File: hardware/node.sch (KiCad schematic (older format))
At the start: 3 parts, among them U1 NRF24L01_Breakout, U2 BluePill_STM32F103C, U3 TM1637_MODULE

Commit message: Add vero desgin to hardware
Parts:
- removed U3: TM1637_MODULE, symbol TinkerForge:TM1637_MODULE
- added U3: TM1637_MODULE, SIP4, symbol bluepill_ups-rescue:TM1637_MODULE
- U1: footprint RF_Module:nRF24L01_Breakout -> SIP8; symbol Bluepill:NRF24L01_Breakout -> bluepill_ups-rescue:NRF24L01_Breakout-Bluepill
- U2: footprint BluePill_breakouts:BluePill_STM32F103C -> BLUEPILL; symbol Bluepill:BluePill_STM32F103C -> bluepill_ups-rescue:BluePill_STM32F103C-Bluepill
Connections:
- net +3V3: now also U2.18 (VCC3V3); no longer U2.40 (VCC3V3)
- net +5V: now also U3.3 (Vcc)
- net GNDREF: now also U3.4 (GND)
- net I2C1_SCL: now also U2.34 (PB6_SCL1); no longer U2.37 (PB9)
- net I2C1_SDA: now also U2.35 (PB7_SDA1); no longer U2.36 (PB8)
- new net: U2.36 (PB8), U3.1 (DIO)
- new net: U2.37 (PB9), U3.2 (CLK)
- no-connect marks 25 -> 23
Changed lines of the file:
@@
 EESchema Schematic File Version 4
+LIBS:bluepill_ups-cache
 EELAYER 26 0
 EELAYER END
@@
 $EndDescr
 $Comp
-L Bluepill:BluePill_STM32F103C U?
-U 1 1 5C14BC04
-P 5650 3750
-AR Path="/5C14BC04" Ref="U?"  Part="1"
-AR Path="/5C14BAF9/5C14BC04" Ref="U2"  Part="1"
-F 0 "U2" H 5675 2278 50  0000 C CNN
-F 1 "BluePill_STM32F103C" H 5675 2187 50  0000 C CNN
-F 2 "BluePill_breakouts:BluePill_STM32F103C" H 5700 2150 50  0001 C CNN
-F 3 "www.rogerclark.net" H 5650 2250 50  0001 C CNN
-	1    5650 3750
-	1    0    0    -1
-$EndComp
-Text Label 7650 3350 0    50   ~ 0
-I2C1_SCL
-Text Label 7650 3450 0    50   ~ 0
-I2C1_SDA
-$Comp
-L TinkerForge:TM1637_MODULE U?
-U 1 1 5C14BC0D
-P 8950 3650
-AR Path="/5C14BC0D" Ref="U?"  Part="1"
-AR Path="/5C14BAF9/5C14BC0D" Ref="U3"  Part="1"
-F 0 "U3" H 8550 4100 60  0000 L CNN
-F 1 "TM1637_MODULE" H 8900 3800 60  0000 L CNN
-F 2 "" H 8950 3650 60  0001 C CNN
-F 3 "" H 8950 3650 60  0000 C CNN
-	1    8950 3650
-	1    0    0    -1
-$EndComp
-Wire Wire Line
-	6550 3350 8350 3350
-Wire Wire Line
-	6550 3450 8350 3450
-Wire Wire Line
-	8350 3550 8250 3550
-Wire Wire Line
-	8250 3550 8250 2900
-$Comp
-L power:GNDREF #PWR?
-U 1 1 5C14BC18
-P 8250 4000
-AR Path="/5C14BC18" Ref="#PWR?"  Part="1"
-AR Path="/5C14BAF9/5C14BC18" Ref="#PWR0101"  Part="1"
-F 0 "#PWR0101" H 8250 3750 50  0001 C CNN
-F 1 "GNDREF" H 8255 3827 50  0001 C CNN
-F 2 "" H 8250 4000 50  0001 C CNN
-F 3 "" H 8250 4000 50  0001 C CNN
-	1    8250 4000
-	1    0    0    -1
-$EndComp
-Wire Wire Line
-	8350 3650 8250 3650
-Wire Wire Line
-	8250 3650 8250 4000
-$Comp
-L Bluepill:NRF24L01_Breakout U?
+L bluepill_ups-rescue:NRF24L01_Breakout-Bluepill U?
 U 1 1 5C14BC20
 P 2150 4150
@@
 F 0 "U1" H 2628 4128 50  0000 L CNN
 F 1 "NRF24L01_Breakout" H 2628 4037 50  0000 L CNN
-F 2 "RF_Module:nRF24L01_Breakout" H 2300 4750 50  0001 L CIN
+F 2 "SIP8" H 2300 4750 50  0001 L CIN
 F 3 "http://www.nordicsemi.com/eng/content/download/2730/34105/file/nRF24L01_Product_Specification_v2_0.pdf" H 2150 4050 50  0001 C CNN
 	1    2150 4150
@@
 	1    0    0    -1
 $EndComp
-$Comp
-L power:+5V #PWR?
-U 1 1 5C14BC3A
-P 6650 3250
-AR Path="/5C14BC3A" Ref="#PWR?"  Part="1"
-AR Path="/5C14BAF9/5C14BC3A" Ref="#PWR0104"  Part="1"
-F 0 "#PWR0104" H 6650 3100 50  0001 C CNN
-F 1 "+5V" V 6650 3400 50  0000 L CNN
-F 2 "" H 6650 3250 50  0001 C CNN
-F 3 "" H 6650 3250 50  0001 C CNN
-	1    6650 3250
-	0    1    1    0
-$EndComp
-$Comp
-L power:GNDREF #PWR?
-U 1 1 5C14BC40
-P 7000 3150
-AR Path="/5C14BC40" Ref="#PWR?"  Part="1"
-AR Path="/5C14BAF9/5C14BC40" Ref="#PWR0105"  Part="1"
-F 0 "#PWR0105" H 7000 2900 50  0001 C CNN
-F 1 "GNDREF" H 7005 2977 50  0001 C CNN
-F 2 "" H 7000 3150 50  0001 C CNN
-F 3 "" H 7000 3150 50  0001 C CNN
-	1    7000 3150
-	0    -1   -1   0
-$EndComp
-Wire Wire Line
-	7000 3150 6550 3150
-Wire Wire Line
-	6650 3250 6550 3250
 Text Label 3250 3850 0    50   ~ 0
 SP1_CS
@@
 L power:+3.3V #PWR?
 U 1 1 5C14BC55
-P 6650 3050
+P 4400 4750
 AR Path="/5C14BC55" Ref="#PWR?"  Part="1"
 AR Path="/5C14BAF9/5C14BC55" Ref="#PWR0107"  Part="1"
-F 0 "#PWR0107" H 6650 2900 50  0001 C CNN
-F 1 "+3.3V" V 6665 3178 50  0000 L CNN
-F 2 "" H 6650 3050 50  0001 C CNN
-F 3 "" H 6650 3050 50  0001 C CNN
-	1    6650 3050
-	0    1    1    0
+F 0 "#PWR0107" H 4400 4600 50  0001 C CNN
+F 1 "+3.3V" V 4415 4878 50  0000 L CNN
+F 2 "" H 4400 4750 50  0001 C CNN
+F 3 "" H 4400 4750 50  0001 C CNN
+	1    4400 4750
+	0    -1   -1   0
 $EndComp
 $Comp
@@
 	4650 4950 4650 5050
 Wire Wire Line
-	4800 3450 3350 3450
-Wire Wire Line
-	4800 3550 3350 3550
-Text HLabel 3350 3450 0    50   Input ~ 0
+	4800 3450 4300 3450
+Wire Wire Line
+	4800 3550 4300 3550
+Text HLabel 4300 3450 0    50   Input ~ 0
 ADC_CH0
-Text HLabel 3350 3550 0    50   Input ~ 0
+Text HLabel 4300 3550 0    50   Input ~ 0
 ADC_CH1
-Wire Wire Line
-	6550 3050 6650 3050
-NoConn ~ 6550 3550
-NoConn ~ 6550 3650
 NoConn ~ 6550 3750
 NoConn ~ 6550 3850
@@
 NoConn ~ 6550 4850
 NoConn ~ 6550 4950
-NoConn ~ 4800 4750
 NoConn ~ 4800 4650
 NoConn ~ 4800 4550
@@
 Text HLabel 7400 4450 2    50   Output ~ 0
 UART1_TX
+$Comp
+L bluepill_ups-rescue:TM1637_MODULE U3
+U 1 1 5C1386FF
+P 9100 3150
+F 0 "U3" H 8700 3000 60  0000 C CNN
+F 1 "TM1637_MODULE" H 9300 3300 60  0000 C CNN
+F 2 "SIP4" H 9193 2969 60  0001 C CNN
+F 3 "" H 9100 3150 60  0000 C CNN
+	1    9100 3150
+	1    0    0    1
+$EndComp
+Wire Wire Line
+	8500 3250 8250 3250
+Wire Wire Line
+	8250 2900 8250 3250
+Wire Wire Line
+	6550 3250 8250 3250
+Connection ~ 8250 3250
+Wire Wire Line
+	6550 3150 7450 3150
+Wire Wire Line
+	7450 3150 7450 3500
+Connection ~ 7450 3150
+Wire Wire Line
+	7450 3150 8500 3150
+$Comp
+L power:GNDREF #PWR?
+U 1 1 5C139F23
+P 7450 3500
+AR Path="/5C139F23" Ref="#PWR?"  Part="1"
+AR Path="/5C14BAF9/5C139F23" Ref="#PWR0101"  Part="1"
+F 0 "#PWR0101" H 7450 3250 50  0001 C CNN
+F 1 "GNDREF" H 7455 3327 50  0001 C CNN
+F 2 "" H 7450 3500 50  0001 C CNN
+F 3 "" H 7450 3500 50  0001 C CNN
+	1    7450 3500
+	1    0    0    -1
+$EndComp
+Wire Wire Line
+	6550 3350 8500 3350
+Wire Wire Line
+	6550 3450 8500 3450
+$Comp
+L bluepill_ups-rescue:BluePill_STM32F103C-Bluepill U?
+U 1 1 5C14BC04
+P 5650 3750
+AR Path="/5C14BC04" Ref="U?"  Part="1"
+AR Path="/5C14BAF9/5C14BC04" Ref="U2"  Part="1"
+F 0 "U2" H 5675 2278 50  0000 C CNN
+F 1 "BluePill_STM32F103C" H 5675 2187 50  0000 C CNN
+F 2 "BLUEPILL" H 5700 2150 50  0001 C CNN
+F 3 "www.rogerclark.net" H 5650 2250 50  0001 C CNN
+	1    5650 3750
+	1    0    0    -1
+$EndComp
+Wire Wire Line
+	4800 4750 4400 4750
+NoConn ~ 6550 3050
+Text HLabel 6700 3650 2    50   BiDi ~ 0
+I2C1_SCL
+Text HLabel 6700 3550 2    50   BiDi ~ 0
+I2C1_SDA
+Wire Wire Line
+	6550 3550 6700 3550
+Wire Wire Line
+	6550 3650 6700 3650
 $EndSCHEMATC

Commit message: ADC actually use averaged values
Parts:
- U1: symbol bluepill_ups-rescue:NRF24L01_Breakout-Bluepill -> bluepill_ups-rescue:NRF24L01_Breakout-Bluepill-bluepill_ups-rescue
- U2: symbol bluepill_ups-rescue:BluePill_STM32F103C-Bluepill -> bluepill_ups-rescue:BluePill_STM32F103C-Bluepill-bluepill_ups-rescue
- U3: symbol bluepill_ups-rescue:TM1637_MODULE -> bluepill_ups-rescue:TM1637_MODULE-bluepill_ups-rescue
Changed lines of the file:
@@
 $EndDescr
 $Comp
-L bluepill_ups-rescue:NRF24L01_Breakout-Bluepill U?
+L bluepill_ups-rescue:NRF24L01_Breakout-Bluepill-bluepill_ups-rescue U?
 U 1 1 5C14BC20
 P 2150 4150
@@
 UART1_TX
 $Comp
-L bluepill_ups-rescue:TM1637_MODULE U3
+L bluepill_ups-rescue:TM1637_MODULE-bluepill_ups-rescue U3
 U 1 1 5C1386FF
 P 9100 3150
@@
 	6550 3450 8500 3450
 $Comp
-L bluepill_ups-rescue:BluePill_STM32F103C-Bluepill U?
+L bluepill_ups-rescue:BluePill_STM32F103C-Bluepill-bluepill_ups-rescue U?
 U 1 1 5C14BC04
 P 5650 3750

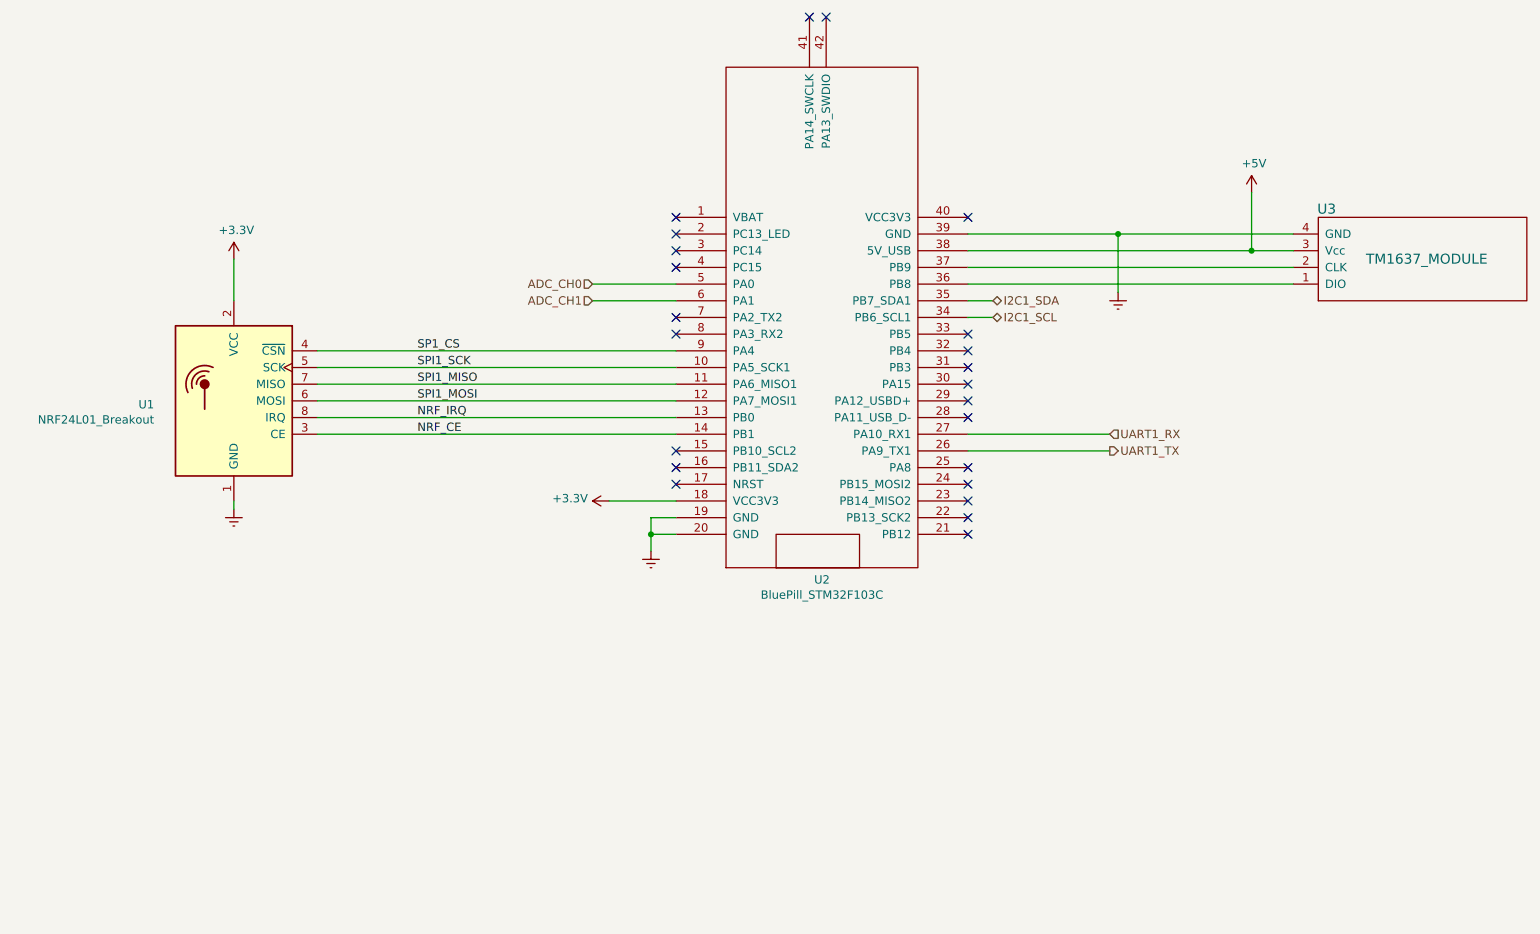
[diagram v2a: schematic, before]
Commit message: Move both UPS to this node
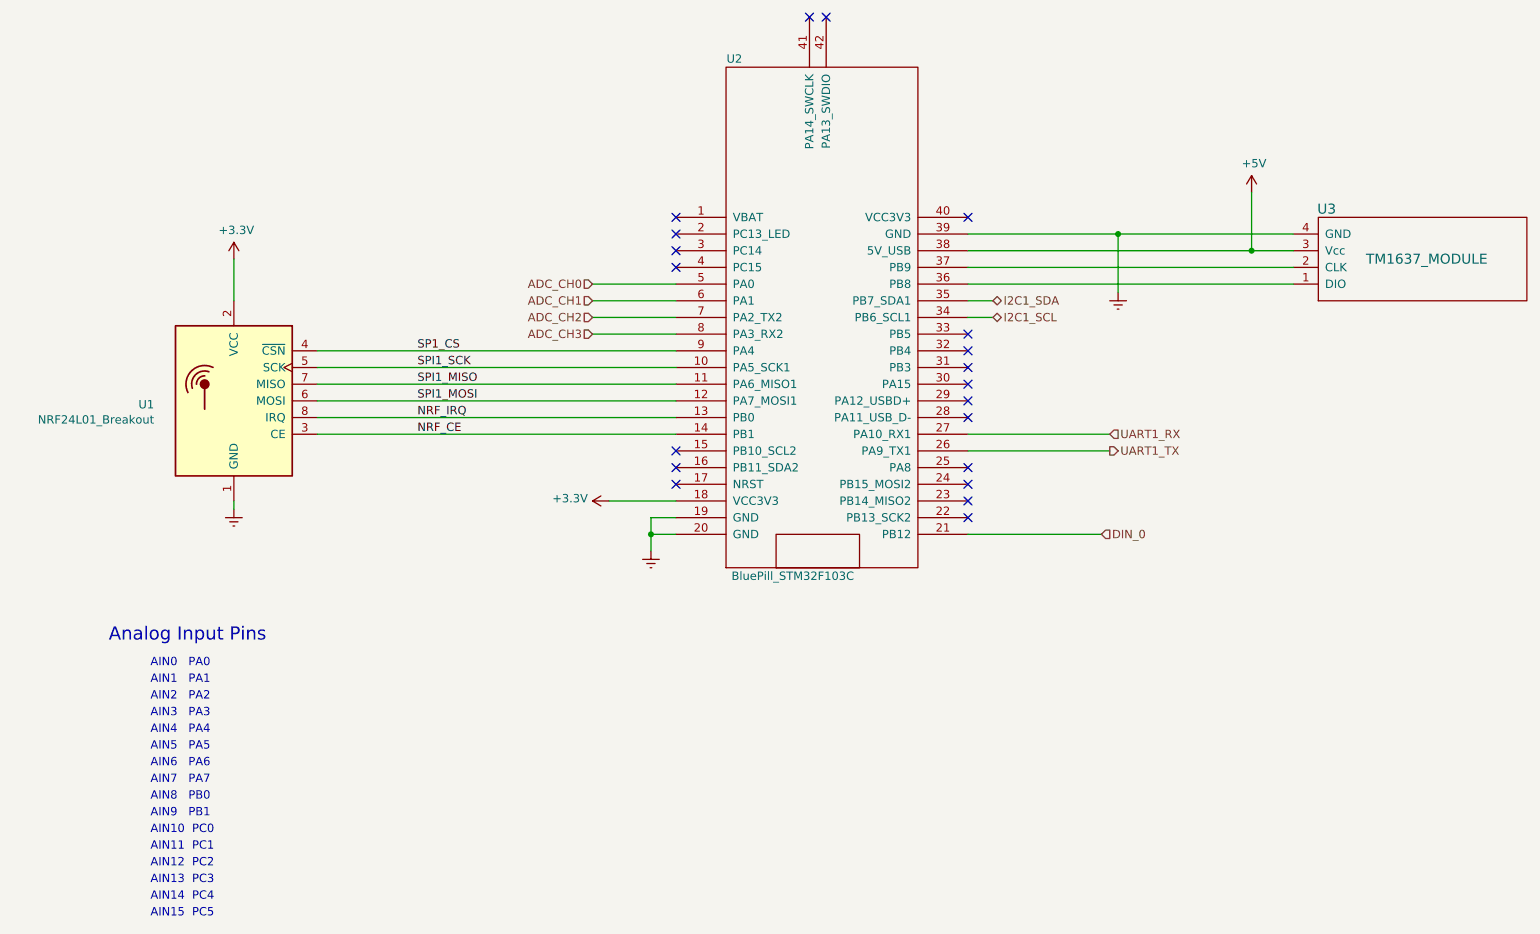
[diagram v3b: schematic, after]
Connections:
- net DIN_0: now reaches U2.21 (PB12)
- net ADC_CH2: now reaches U2.7 (PA2_TX2)
- net ADC_CH3: now reaches U2.8 (PA3_RX2)
- no-connect marks 23 -> 20
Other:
- note added: "AIN0 PA0"
- note added: "AIN1 PA1"
- note added: "AIN10 PC0"
- note added: "AIN11 PC1"
- note added: "AIN12 PC2"
- note added: "AIN13 PC3"
- note added: "AIN14 PC4"
- note added: "AIN15 PC5"
- note added: "AIN2 PA2"
- note added: "AIN3 PA3"
- note added: "AIN4 PA4"
- note added: "AIN5 PA5"
- note added: "AIN6 PA6"
- note added: "AIN7 PA7"
- note added: "AIN8 PB0"
- note added: "AIN9 PB1"
- note added: "Analog Input Pins"
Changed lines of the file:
@@
 Sheet 2 2
 Title "RF Node"
-Date "2018-12-14"
+Date "2019-12-21"
 Rev ""
 Comp ""
@@
 NoConn ~ 6550 4750
 NoConn ~ 6550 4850
-NoConn ~ 6550 4950
 NoConn ~ 4800 4650
 NoConn ~ 4800 4550
 NoConn ~ 4800 4450
-NoConn ~ 4800 3750
-NoConn ~ 4800 3650
 NoConn ~ 4800 3350
 NoConn ~ 4800 3250
@@
 AR Path="/5C14BC04" Ref="U?"  Part="1"
 AR Path="/5C14BAF9/5C14BC04" Ref="U2"  Part="1"
-F 0 "U2" H 5675 2278 50  0000 C CNN
-F 1 "BluePill_STM32F103C" H 5675 2187 50  0000 C CNN
+F 0 "U2" H 5150 5400 50  0000 C CNN
+F 1 "BluePill_STM32F103C" H 5500 2300 50  0000 C CNN
 F 2 "BLUEPILL" H 5700 2150 50  0001 C CNN
 F 3 "www.rogerclark.net" H 5650 2250 50  0001 C CNN
@@
 Wire Wire Line
 	6550 3650 6700 3650
+Text Notes 1400 5600 0    79   ~ 0
+Analog Input Pins
+Text Notes 1650 5750 0    50   ~ 0
+AIN0   PA0
+Text Notes 1650 5850 0    50   ~ 0
+AIN1   PA1
+Text Notes 1650 5950 0    50   ~ 0
+AIN2   PA2
+Text Notes 1650 6050 0    50   ~ 0
+AIN3   PA3
+Text Notes 1650 6150 0    50   ~ 0
+AIN4   PA4
+Text Notes 1650 6250 0    50   ~ 0
+AIN5   PA5
+Text Notes 1650 6350 0    50   ~ 0
+AIN6   PA6
+Text Notes 1650 6450 0    50   ~ 0
+AIN7   PA7
+Text Notes 1650 6550 0    50   ~ 0
+AIN8   PB0
+Text Notes 1650 6650 0    50   ~ 0
+AIN9   PB1
+Text Notes 1650 6750 0    50   ~ 0
+AIN10  PC0
+Text Notes 1650 6850 0    50   ~ 0
+AIN11  PC1
+Text Notes 1650 6950 0    50   ~ 0
+AIN12  PC2
+Text Notes 1650 7050 0    50   ~ 0
+AIN13  PC3
+Text Notes 1650 7150 0    50   ~ 0
+AIN14  PC4
+Text Notes 1650 7250 0    50   ~ 0
+AIN15  PC5
+Text HLabel 4300 3650 0    50   Input ~ 0
+ADC_CH2
+Text HLabel 4300 3750 0    50   Input ~ 0
+ADC_CH3
+Wire Wire Line
+	4300 3650 4800 3650
+Wire Wire Line
+	4300 3750 4800 3750
+Wire Wire Line
+	6550 4950 7350 4950
+Text HLabel 7350 4950 2    50   Input ~ 0
+DIN_0
 $EndSCHEMATC
